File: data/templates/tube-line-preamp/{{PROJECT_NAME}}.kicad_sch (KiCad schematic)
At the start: 14 parts, among them X1 6N2P, X2 6N2P

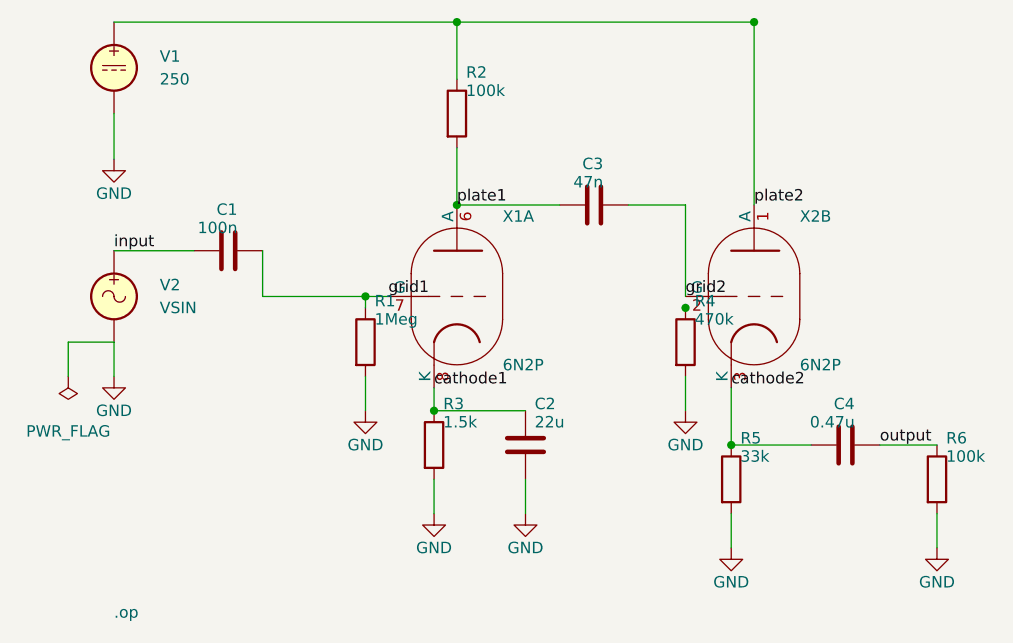
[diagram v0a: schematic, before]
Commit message: T029 Phase 0: fix 4 dirty templates via builders
Builders (active-lpf-sallen-key, op-amp-inverting, bjt-ce-nfb) add a
PWR_FLAG on the GND net to clear ERC `power_pin_not_driven`. The
tube-line-preamp builder fixes r_g2.pin_b wiring — previous connect
target (114.3, 90.17) was the pin's own coordinate (zero-length wire),
leaving R4 pin 1 floating; new target (114.3, 88.9) places it on the
grid2 net as a canonical grid-leak.

data/templates/* regenerated via scripts/regenerate-templates.py. All
11 templates now ERC-clean (errors=0) — satisfies T029 SC1.

Calibration baselines for tube-line-preamp updated to reflect the now
correctly-biased CF: V_cathode2 window 30-150V → 2-50V; mid-band gain
baseline 64.0 → 54.0 V/V (matches analytical 54 V/V hand-calc exactly,
which is now achievable because R4 grid-leak loads C3→V1B coupling per
hand-calc assumption).

Spec §6 A1 amended: fix path is "via builders + regen", not direct
edits to data/templates/. Direct-edit probe (2026-06-05) confirmed
0-errors achievable but breaks snapshot tests and is wiped by next
regenerate-templates.py.

Pre-push 5/5 ✓ (ruff/format/mypy clean; 2025 passed, 10 skipped,
1 xfailed; coverage 86.98%).

Co-Authored-By: Claude Opus 4.7 (1M context) <noreply@anthropic.com>
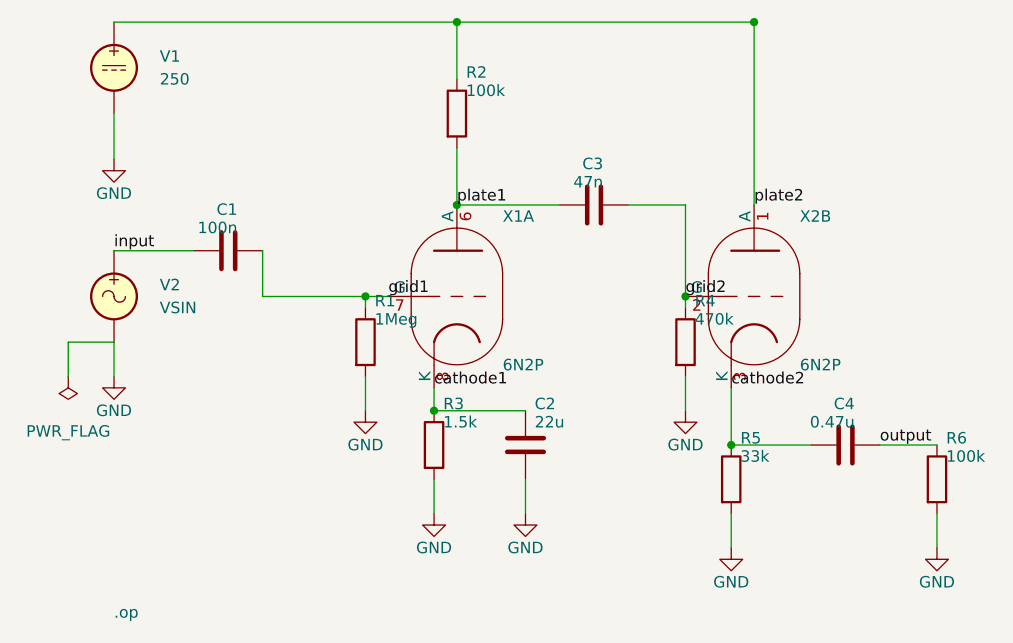
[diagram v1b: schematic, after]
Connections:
- net grid2: now also R4.1
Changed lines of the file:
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@@
+	(wire
+		(pts
+			(xy 114.3 90.17) (xy 114.3 88.9)
+		)
+		(stroke
+			(width 0)
+			(type default)
+		)
+	)
 	(wire
 		(pts
@@
 	)
 	(junction
-		(at 114.3 90.17)
+		(at 114.3 88.9)
 		(diameter 0)
 		(color 0 0 0 0)
